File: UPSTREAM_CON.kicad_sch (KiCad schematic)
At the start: 11 parts, among them J3 USB3_A, U6 TPD6E05U06RVZ, U7 LM66100DCK

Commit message: Arbeit
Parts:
- added R5: R, symbol Device:R
- C1, C2: footprint (none) -> Capacitor_SMD:C_0603_1608Metric
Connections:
- net +5V: now also R5.1
- net GND: no longer U7.5 (ST)
- net USB_UP_SSTX_C_N: no longer C5.2
- net USB_UP_SSTX_C_P: no longer C6.2
- new net USB_UP_PORT_POWER_ON: R5.2, U7.5 (ST)
- new net USB_UP_SSRX_C_N: C5.2
- new net USB_UP_SSRX_C_P: C6.2
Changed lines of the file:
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@@
+	)
+	(junction
+		(at 147.32 60.96)
+		(diameter 0)
+		(color 0 0 0 0)
 	)
 	(junction
@@
 		(color 0 0 0 0)
 	)
+	(junction
+		(at 147.32 50.8)
+		(diameter 0)
+		(color 0 0 0 0)
+	)
 	(no_connect
 		(at 63.5 109.22)
@@
 	(wire
 		(pts
+			(xy 147.32 60.96) (xy 142.24 60.96)
+		)
+		(stroke
+			(width 0)
+			(type default)
+		)
+	)
+	(wire
+		(pts
 			(xy 140.97 144.78) (xy 161.29 144.78)
 		)
@@
 	(wire
 		(pts
+			(xy 147.32 60.96) (xy 147.32 59.69)
+		)
+		(stroke
+			(width 0)
+			(type default)
+		)
+	)
+	(wire
+		(pts
 			(xy 99.06 50.8) (xy 99.06 55.88)
 		)
@@
 	(wire
 		(pts
-			(xy 139.7 55.88) (xy 138.43 55.88)
+			(xy 138.43 55.88) (xy 142.24 55.88)
 		)
 		(stroke
@@
 	(wire
 		(pts
+			(xy 147.32 52.07) (xy 147.32 50.8)
+		)
+		(stroke
+			(width 0)
+			(type default)
+		)
+	)
+	(wire
+		(pts
 			(xy 140.97 165.1) (xy 161.29 165.1)
 		)
@@
 	(wire
 		(pts
+			(xy 147.32 60.96) (xy 161.29 60.96)
+		)
+		(stroke
+			(width 0)
+			(type default)
+		)
+	)
+	(wire
+		(pts
 			(xy 222.25 105.41) (xy 231.14 105.41)
 		)
@@
 	(wire
 		(pts
+			(xy 142.24 55.88) (xy 142.24 60.96)
+		)
+		(stroke
+			(width 0)
+			(type default)
+		)
+	)
+	(wire
+		(pts
 			(xy 82.55 81.28) (xy 82.55 50.8)
 		)
@@
 	(wire
 		(pts
-			(xy 139.7 60.96) (xy 139.7 55.88)
-		)
-		(stroke
-			(width 0)
-			(type default)
-		)
-	)
-	(wire
-		(pts
 			(xy 140.97 149.86) (xy 161.29 149.86)
 		)
@@
 	(wire
 		(pts
+			(xy 147.32 50.8) (xy 153.67 50.8)
+		)
+		(stroke
+			(width 0)
+			(type default)
+		)
+	)
+	(wire
+		(pts
 			(xy 87.63 69.85) (xy 87.63 63.5)
 		)
@@
 	(wire
 		(pts
-			(xy 138.43 50.8) (xy 153.67 50.8)
+			(xy 138.43 50.8) (xy 147.32 50.8)
 		)
 		(stroke
@@
 			)
 			(justify right bottom)
+		)
+	)
+	(hierarchical_label "USB_UP_PORT_POWER_ON"
+		(shape output)
+		(at 161.29 60.96 0)
+		(effects
+			(font
+				(size 1.27 1.27)
+			)
+			(justify left)
 		)
 	)
@@
 		)
 	)
-	(hierarchical_label "USB_UP_SSTX_C_P"
+	(hierarchical_label "USB_UP_SSRX_C_P"
 		(shape output)
 		(at 231.14 100.33 0)
@@
 		)
 	)
-	(hierarchical_label "USB_UP_SSTX_C_N"
+	(hierarchical_label "USB_UP_SSRX_C_N"
 		(shape output)
 		(at 231.14 95.25 0)
@@
 				(path "/96aa4cdc-6548-43b6-b96a-6d1618c17d83/c2937931-474a-4fd2-9f5c-ad5f88abb5b8"
 					(reference "#PWR018")
+					(unit 1)
+				)
+			)
+		)
+	)
+	(symbol
+		(lib_id "Device:R")
+		(at 147.32 55.88 0)
+		(unit 1)
+		(exclude_from_sim no)
+		(in_bom yes)
+		(on_board yes)
+		(dnp no)
+		(property "Reference" "R5"
+			(at 149.86 54.6099 0)
+			(effects
+				(font
+					(size 1.27 1.27)
+				)
+				(justify left)
+			)
+		)
+		(property "Value" "R"
+			(at 149.86 57.1499 0)
+			(effects
+				(font
+					(size 1.27 1.27)
+				)
+				(justify left)
+			)
+		)
+		(property "Footprint" ""
+			(at 145.542 55.88 90)
+			(effects
+				(font
+					(size 1.27 1.27)
+				)
+				(hide yes)
+			)
+		)
+		(property "Datasheet" "~"
+			(at 147.32 55.88 0)
+			(effects
+				(font
+					(size 1.27 1.27)
+				)
+				(hide yes)
+			)
+		)
+		(property "Description" "Resistor"
+			(at 147.32 55.88 0)
+			(effects
+				(font
+					(size 1.27 1.27)
+				)
+				(hide yes)
+			)
+		)
+		(pin "1"
+		)
+		(pin "2"
+		)
+		(instances
+			(project "USB_3_SWITCHER"
+				(path "/96aa4cdc-6548-43b6-b96a-6d1618c17d83/c2937931-474a-4fd2-9f5c-ad5f88abb5b8"
+					(reference "R5")
 					(unit 1)
 				)
@@
 			)
 		)
-		(property "Footprint" ""
+		(property "Footprint" "Capacitor_SMD:C_0603_1608Metric"
 			(at 88.5952 63.5 0)
 			(effects
@@
 	)
 	(symbol
-		(lib_id "power:GND")
-		(at 139.7 60.96 0)
-		(unit 1)
-		(exclude_from_sim no)
-		(in_bom yes)
-		(on_board yes)
-		(dnp no)
-		(fields_autoplaced yes)
-		(property "Reference" "#PWR015"
-			(at 139.7 67.31 0)
-			(effects
-				(font
-					(size 1.27 1.27)
-				)
-				(hide yes)
-			)
-		)
-		(property "Value" "GND"
-			(at 139.7 66.04 0)
-			(effects
-				(font
-					(size 1.27 1.27)
-				)
-			)
-		)
-		(property "Footprint" ""
-			(at 139.7 60.96 0)
-			(effects
-				(font
-					(size 1.27 1.27)
-				)
-				(hide yes)
-			)
-		)
-		(property "Datasheet" ""
-			(at 139.7 60.96 0)
-			(effects
-				(font
-					(size 1.27 1.27)
-				)
-				(hide yes)
-			)
-		)
-		(property "Description" "Power symbol creates a global label with name \"GND\" , ground"
-			(at 139.7 60.96 0)
-			(effects
-				(font
-					(size 1.27 1.27)
-				)
-				(hide yes)
-			)
-		)
-		(pin "1"
-		)
-		(instances
-			(project "USB_3_SWITCHER"
-				(path "/96aa4cdc-6548-43b6-b96a-6d1618c17d83/c2937931-474a-4fd2-9f5c-ad5f88abb5b8"
-					(reference "#PWR015")
-					(unit 1)
-				)
-			)
-		)
-	)
-	(symbol
 		(lib_id "Device:C")
 		(at 99.06 59.69 0)
@@
 			)
 		)
-		(property "Footprint" ""
+		(property "Footprint" "Capacitor_SMD:C_0603_1608Metric"
 			(at 100.0252 63.5 0)
 			(effects

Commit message: Weiter gearbeitet
Fast fertig:
HUB
Fertig
Connector (Up and Down)
MUX
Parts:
- added C14: 10u, Capacitor_SMD:C_0603_1608Metric, symbol Device:C
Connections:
- net +5V: now also C14.1
- net GND: now also C14.2
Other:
- moved on the sheet: C5, C6, C7, C8, U6

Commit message: Footprints Updated
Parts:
- C1, C14, C2: footprint Capacitor_SMD:C_0603_1608Metric -> 00_Capacitor:Cap_0603
- C5, C6, C7, C8: footprint (none) -> 00_Capacitor:Cap_0402
- J3: footprint Crystal:Crystal_SMD_WE_CFPX-180-4Pin_3.2x2.5mm -> (none)
- R1, R2, R5: footprint (none) -> 00_Resistor:Res_0402
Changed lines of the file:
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@@
 			)
 		)
-		(property "Footprint" ""
+		(property "Footprint" "00_Resistor:Res_0402"
 			(at 145.542 55.88 90)
 			(effects
@@
 			)
 		)
-		(property "Footprint" ""
+		(property "Footprint" "00_Capacitor:Cap_0402"
 			(at 177.8 104.14 0)
 			(effects
@@
 			)
 		)
-		(property "Footprint" ""
+		(property "Footprint" "00_Capacitor:Cap_0402"
 			(at 171.45 101.6 0)
 			(effects
@@
 			)
 		)
-		(property "Footprint" ""
+		(property "Footprint" "00_Resistor:Res_0402"
 			(at 109.982 54.61 90)
 			(effects
@@
 			)
 		)
-		(property "Footprint" ""
+		(property "Footprint" "00_Capacitor:Cap_0402"
 			(at 171.45 93.98 0)
 			(effects
@@
 			)
 		)
-		(property "Footprint" "Capacitor_SMD:C_0603_1608Metric"
+		(property "Footprint" "00_Capacitor:Cap_0603"
 			(at 88.5952 63.5 0)
 			(effects
@@
 			)
 		)
-		(property "Footprint" "Capacitor_SMD:C_0603_1608Metric"
+		(property "Footprint" "00_Capacitor:Cap_0603"
 			(at 100.0252 63.5 0)
 			(effects
@@
 			)
 		)
-		(property "Footprint" ""
+		(property "Footprint" "00_Capacitor:Cap_0402"
 			(at 177.8 96.52 0)
 			(effects
@@
 			)
 		)
-		(property "Footprint" ""
+		(property "Footprint" "00_Resistor:Res_0402"
 			(at 109.982 64.77 90)
 			(effects
@@
 			)
 		)
-		(property "Footprint" "Capacitor_SMD:C_0603_1608Metric"
+		(property "Footprint" "00_Capacitor:Cap_0603"
 			(at 164.7952 50.8 0)
 			(effects
@@
 			)
 		)
-		(property "Footprint" "Crystal:Crystal_SMD_WE_CFPX-180-4Pin_3.2x2.5mm"
+		(property "Footprint" ""
 			(at 69.85 88.9 0)
 			(effects

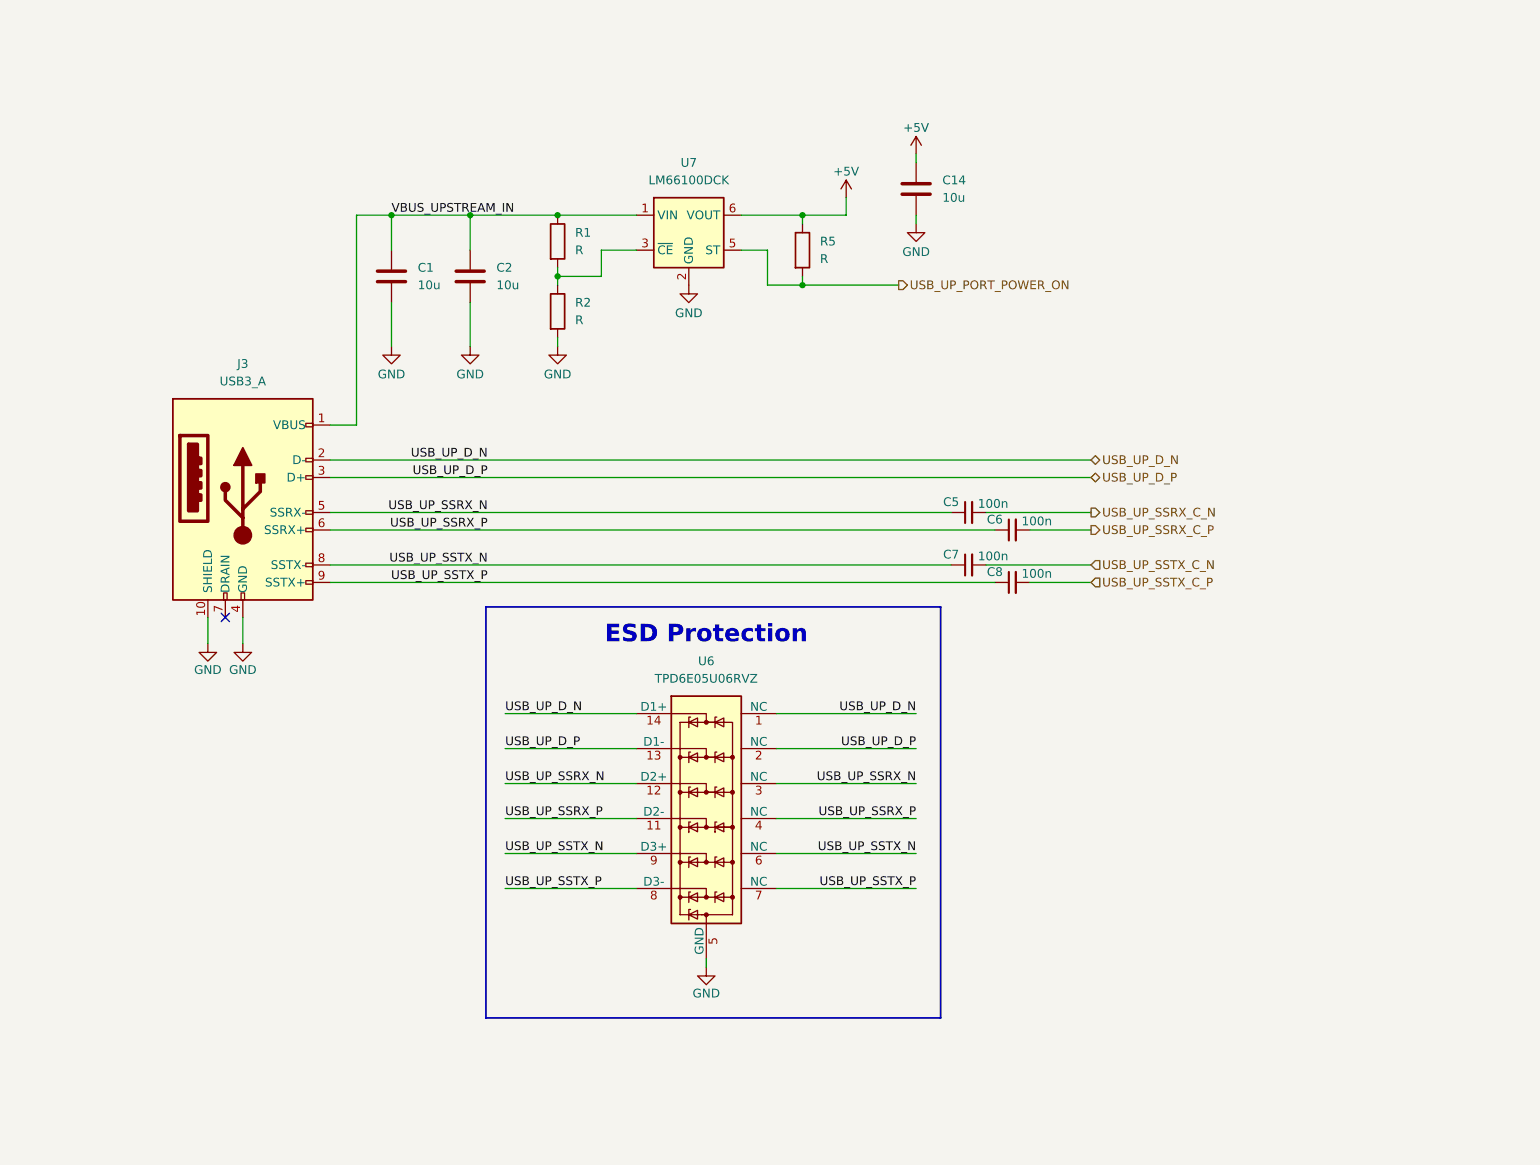
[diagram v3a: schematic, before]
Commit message: USB 3 Stecker ausgetauscht
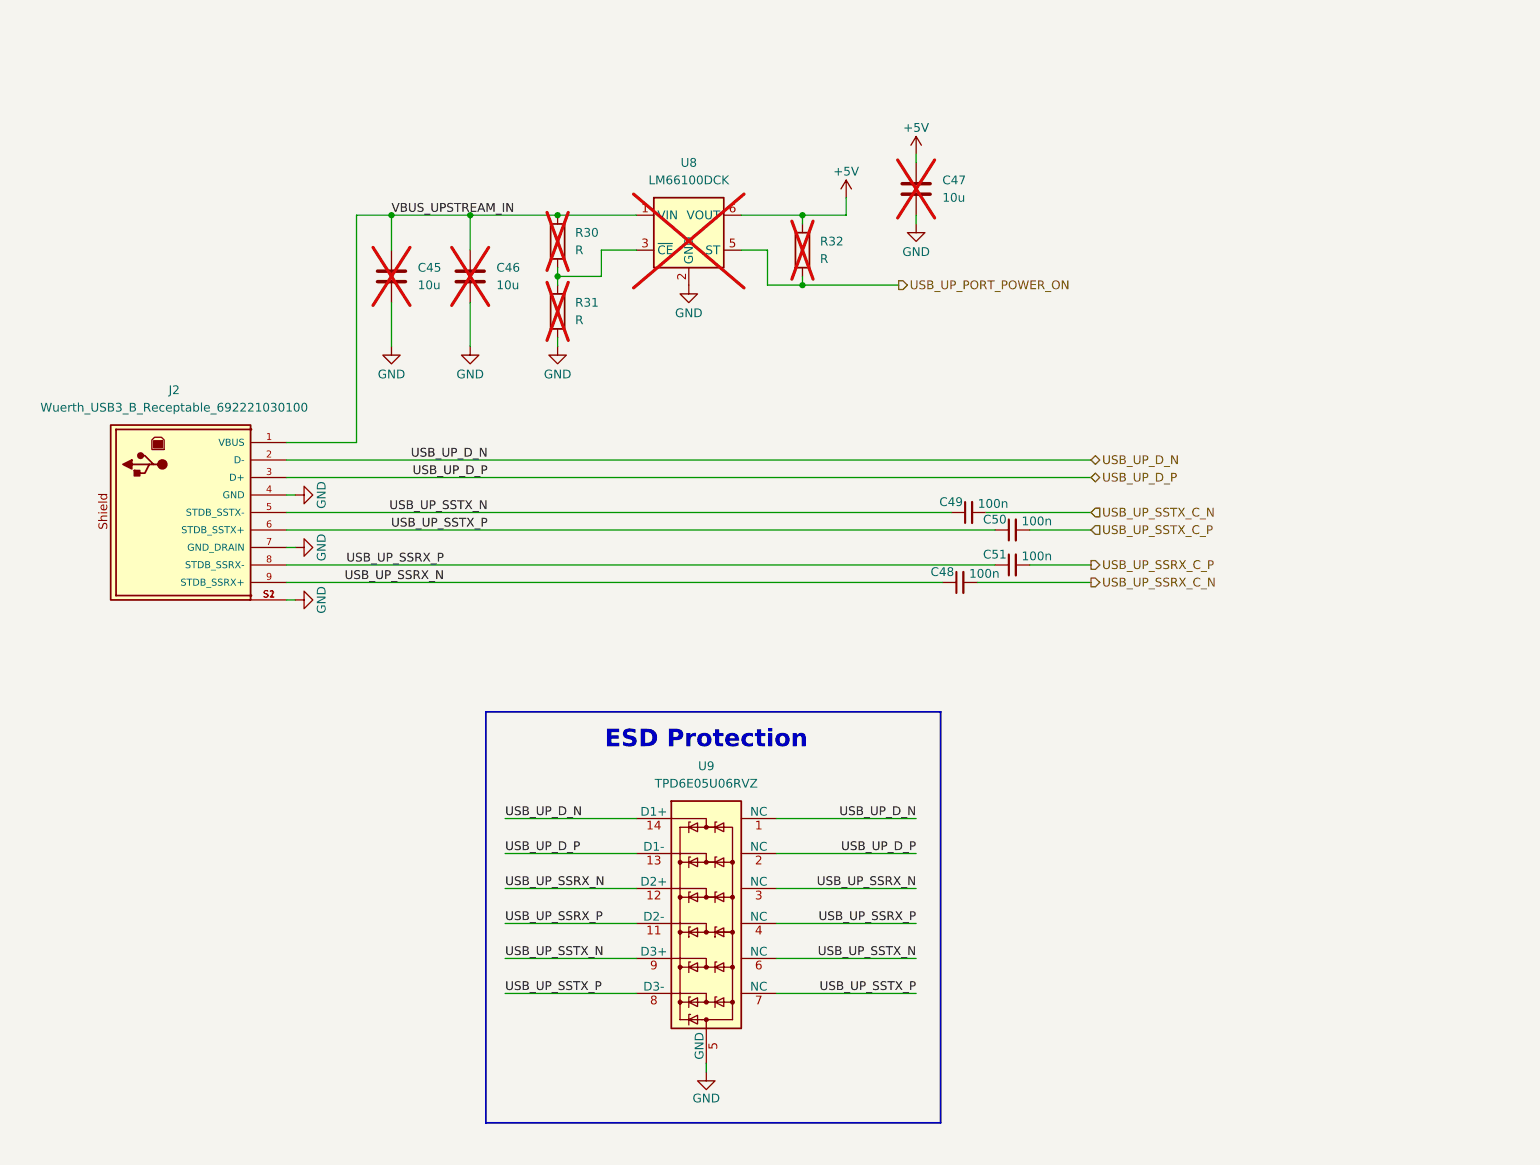
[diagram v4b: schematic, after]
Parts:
- removed J3: USB3_A, symbol Connector:USB3_A
- added J2: Wuerth_USB3_B_Receptable_692221030100, 00_Connector:Wuerth_USB3B_692221030100, symbol 00_Connectors_USB:Wuerth_USB3_B_Receptable_692221030100
- C45: renamed from C1; now not fitted
- C46: renamed from C2; now not fitted
- C47: renamed from C14; now not fitted
- R30: renamed from R1; now not fitted
- R31: renamed from R2; now not fitted
- R32: renamed from R5; now not fitted
- U8: renamed from U7; now not fitted
- renumbered C5 to C48, C7 to C49, C8 to C50, C6 to C51, U6 to U9
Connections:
- net GND: now also J2.4 (GND), J2.7 (GND_DRAIN), J2.S1, J2.S2
- net USB_UP_D_N: now also J2.2 (D-)
- net USB_UP_D_P: now also J2.3 (D+)
- net USB_UP_SSRX_N: now also J2.9 (STDB_SSRX+)
- net USB_UP_SSRX_P: now also J2.8 (STDB_SSRX-)
- net USB_UP_SSTX_N: now also J2.5 (STDB_SSTX-)
- net USB_UP_SSTX_P: now also J2.6 (STDB_SSTX+)
- net VBUS_UPSTREAM_IN: now also J2.1 (VBUS)
- no-connect marks 1 -> 0
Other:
- moved on the sheet: C48, C49, C50, C51, U9

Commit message: Weiter gemacht
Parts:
- added C96: 10u, 00_Capacitor:Cap_0603, symbol Device:C
- added D1: D_Schottky, Diode_SMD:D_SOD-323, symbol Device:D_Schottky
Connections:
- net GND: now also C96.2
- net USB_UP_D_N: now also U9.12 (D2+), U9.3 (NC); no longer U9.1 (NC), U9.14 (D1+)
- net USB_UP_D_P: now also U9.11 (D2-), U9.4 (NC); no longer U9.13 (D1-), U9.2 (NC)
- net USB_UP_SSRX_N: now also U9.1 (NC), U9.14 (D1+); no longer U9.12 (D2+), U9.3 (NC)
- net USB_UP_SSRX_P: now also U9.13 (D1-), U9.2 (NC); no longer U9.11 (D2-), U9.4 (NC)
- net USB_UP_SSTX_N: now also U9.7 (NC), U9.8 (D3-); no longer U9.6 (NC), U9.9 (D3+)
- net USB_UP_SSTX_P: now also U9.6 (NC), U9.9 (D3+); no longer U9.7 (NC), U9.8 (D3-)
- net VBUS_UPSTREAM_IN: now also D1.2 (A)
- new net VBUS: C96.1, D1.1 (K)

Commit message: weiter gemacht
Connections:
- net USB_UP_SSRX_C_N: now also C51.2; no longer C48.2
- net USB_UP_SSRX_C_P: now also C48.2; no longer C51.2
- net USB_UP_SSRX_N: now also C51.1, J2.8 (STDB_SSRX-), U9.13 (D1-), U9.2 (NC); no longer C48.1, J2.9 (STDB_SSRX+), U9.1 (NC), U9.14 (D1+)
- net USB_UP_SSRX_P: now also C48.1, J2.9 (STDB_SSRX+), U9.1 (NC), U9.14 (D1+); no longer C51.1, J2.8 (STDB_SSRX-), U9.13 (D1-), U9.2 (NC)
- net USB_UP_SSTX_N: now also U9.6 (NC), U9.9 (D3+); no longer U9.7 (NC), U9.8 (D3-)
- net USB_UP_SSTX_P: now also U9.7 (NC), U9.8 (D3-); no longer U9.6 (NC), U9.9 (D3+)

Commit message: Weiter gemacht
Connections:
- net USB_UP_SSTX_N: now also U9.7 (NC), U9.8 (D3-); no longer U9.6 (NC), U9.9 (D3+)
- net USB_UP_SSTX_P: now also U9.6 (NC), U9.9 (D3+); no longer U9.7 (NC), U9.8 (D3-)
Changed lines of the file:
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@@
 		)
 	)
-	(label "USB_UP_SSTX_P"
+	(label "USB_UP_SSTX_N"
 		(at 163.83 163.83 180)
 		(effects
@@
 		)
 	)
-	(label "USB_UP_SSTX_P"
+	(label "USB_UP_SSTX_N"
 		(at 104.14 163.83 0)
 		(effects
@@
 		)
 	)
-	(label "USB_UP_SSTX_N"
+	(label "USB_UP_SSTX_P"
 		(at 104.14 158.75 0)
 		(effects
@@
 		)
 	)
-	(label "USB_UP_SSTX_N"
+	(label "USB_UP_SSTX_P"
 		(at 163.83 158.75 180)
 		(effects

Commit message: Layout + Schematic weiter gemacht
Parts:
- removed D1: D_Schottky, Diode_SMD:D_SOD-323, symbol Device:D_Schottky
- added D1: BAT54J, Diode_SMD:D_SOD-323F, symbol Diode:BAT54J
- C96: value 10u -> 1u
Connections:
- net VBUS: now also D1.1 (K)
- net VBUS_UPSTREAM_IN: now also D1.2 (A)
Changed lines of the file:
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@@
 			)
 		)
-		(property "Value" "10u"
+		(property "Value" "1u"
 			(at 149.86 35.5599 0)
 			(show_name no)
@@
 	)
 	(symbol
+		(lib_id "Diode:BAT54J")
+		(at 129.54 35.56 180)
+		(unit 1)
+		(body_style 1)
+		(exclude_from_sim no)
+		(in_bom yes)
+		(on_board yes)
+		(in_pos_files yes)
+		(dnp no)
+		(fields_autoplaced yes)
+		(property "Reference" "D1"
+			(at 129.8575 29.21 0)
+			(show_name no)
+			(do_not_autoplace no)
+			(effects
+				(font
+					(size 1.27 1.27)
+				)
+			)
+		)
+		(property "Value" "BAT54J"
+			(at 129.8575 31.75 0)
+			(show_name no)
+			(do_not_autoplace no)
+			(effects
+				(font
+					(size 1.27 1.27)
+				)
+			)
+		)
+		(property "Footprint" "Diode_SMD:D_SOD-323F"
+			(at 129.54 31.115 0)
+			(hide yes)
+			(show_name no)
+			(do_not_autoplace no)
+			(effects
+				(font
+					(size 1.27 1.27)
+				)
+			)
+		)
+		(property "Datasheet" "https://assets.nexperia.com/documents/data-sheet/BAT54J.pdf"
+			(at 129.54 35.56 0)
+			(hide yes)
+			(show_name no)
+			(do_not_autoplace no)
+			(effects
+				(font
+					(size 1.27 1.27)
+				)
+			)
+		)
+		(property "Description" "30V 200mA Schottky diode, SOD-323F"
+			(at 129.54 35.56 0)
+			(hide yes)
+			(show_name no)
+			(do_not_autoplace no)
+			(effects
+				(font
+					(size 1.27 1.27)
+				)
+			)
+		)
+		(pin "1"
+		)
+		(pin "2"
+		)
+		(instances
+			(project ""
+				(path "/96aa4cdc-6548-43b6-b96a-6d1618c17d83/c2937931-474a-4fd2-9f5c-ad5f88abb5b8"
+					(reference "D1")
+					(unit 1)
+				)
+				(path "/96aa4cdc-6548-43b6-b96a-6d1618c17d83/d10018df-95fc-480c-88d9-89d40f47512d"
+					(reference "D2")
+					(unit 1)
+				)
+			)
+		)
+	)
+	(symbol
 		(lib_id "power:GND")
 		(at 73.66 91.44 90)
@@
 					(unit 1)
 				)
-			)
-		)
-	)
-	(symbol
-		(lib_id "Device:D_Schottky")
-		(at 129.54 35.56 180)
-		(unit 1)
-		(body_style 1)
-		(exclude_from_sim no)
-		(in_bom yes)
-		(on_board yes)
-		(in_pos_files yes)
-		(dnp no)
-		(fields_autoplaced yes)
-		(property "Reference" "D1"
-			(at 129.8575 29.21 0)
-			(show_name no)
-			(do_not_autoplace no)
-			(effects
-				(font
-					(size 1.27 1.27)
-				)
-			)
-		)
-		(property "Value" "D_Schottky"
-			(at 129.8575 31.75 0)
-			(show_name no)
-			(do_not_autoplace no)
-			(effects
-				(font
-					(size 1.27 1.27)
-				)
-			)
-		)
-		(property "Footprint" "Diode_SMD:D_SOD-323"
-			(at 129.54 35.56 0)
-			(hide yes)
-			(show_name no)
-			(do_not_autoplace no)
-			(effects
-				(font
-					(size 1.27 1.27)
-				)
-			)
-		)
-		(property "Datasheet" ""
-			(at 129.54 35.56 0)
-			(hide yes)
-			(show_name no)
-			(do_not_autoplace no)
-			(effects
-				(font
-					(size 1.27 1.27)
-				)
-			)
-		)
-		(property "Description" "Schottky diode"
-			(at 129.54 35.56 0)
-			(hide yes)
-			(show_name no)
-			(do_not_autoplace no)
-			(effects
-				(font
-					(size 1.27 1.27)
-				)
-			)
-		)
-		(pin "2"
-		)
-		(pin "1"
-		)
-		(instances
-			(project ""
-				(path "/96aa4cdc-6548-43b6-b96a-6d1618c17d83/c2937931-474a-4fd2-9f5c-ad5f88abb5b8"
-					(reference "D1")
-					(unit 1)
-				)
-				(path "/96aa4cdc-6548-43b6-b96a-6d1618c17d83/d10018df-95fc-480c-88d9-89d40f47512d"
-					(reference "D2")
-					(unit 1)
-				)
